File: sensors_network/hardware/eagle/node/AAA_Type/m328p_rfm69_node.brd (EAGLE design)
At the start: 50.8 x 41.9 mm, 37 parts, among them IC2 L6920, SW2 Node ID, U1 ATMEGA328P, U2 RFM69W, Y1 8MHz

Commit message: [sensors_network][AAA_Type] final pcb touches
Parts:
- moved R4 0.25 mm to (25.7, 6.60)
- moved JP2 0.25 mm to (19.1, 3.05)
- moved JP4 0.25 mm to (19.1, 6.35)
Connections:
- removed net D5_EXT: JP5.1, SJ1.1
- new net D6_EXT: JP5.2, SJ1.1
- net D5: now also JP5.1; no longer SJ1.2
- net D6: now also SJ1.2; no longer JP5.2
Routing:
- net D5: track 24.9 -> 8.42 mm, vias 2 -> 0
- net D5_EXT: track 9.61 -> 0.00 mm, vias 2 -> 0
- net GND: track 275.5 -> 267.9 mm
- net B1: track 12.2 -> 17.0 mm, vias 0 -> 2
- net D6: track 9.81 -> 6.36 mm
- net D6_EXT: track 0.00 -> 3.21 mm
- net SCK: track 29.4 -> 31.1 mm
- net BATT_LVL: track 38.2 -> 39.7 mm
- net CT_OUT: track 33.2 -> 34.1 mm
- net RESET: track 49.9 -> 50.6 mm
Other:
- board text added: "RF_LED|D6"
- board text removed: "RF_LED|D5"

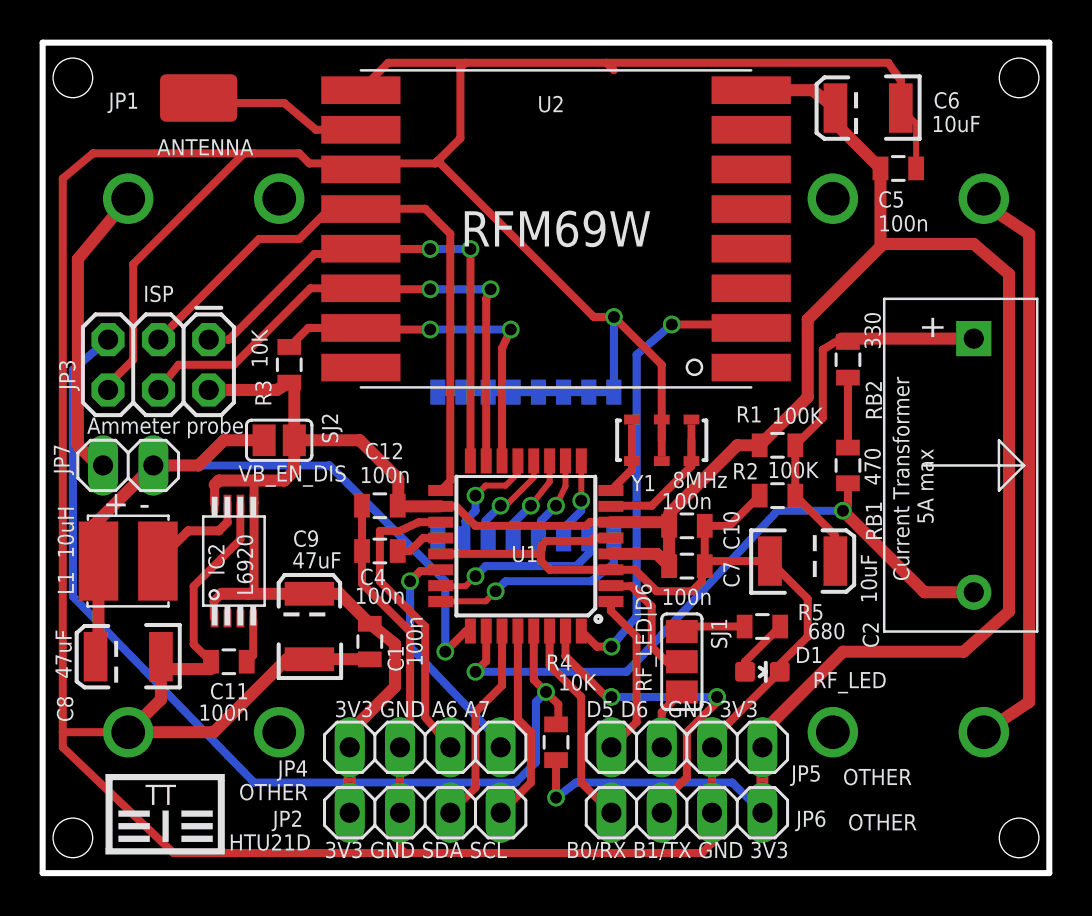
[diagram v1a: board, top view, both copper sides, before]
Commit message: [sensors_network][AAA_Type] reduced board outline dimension to fit 5x5 cm
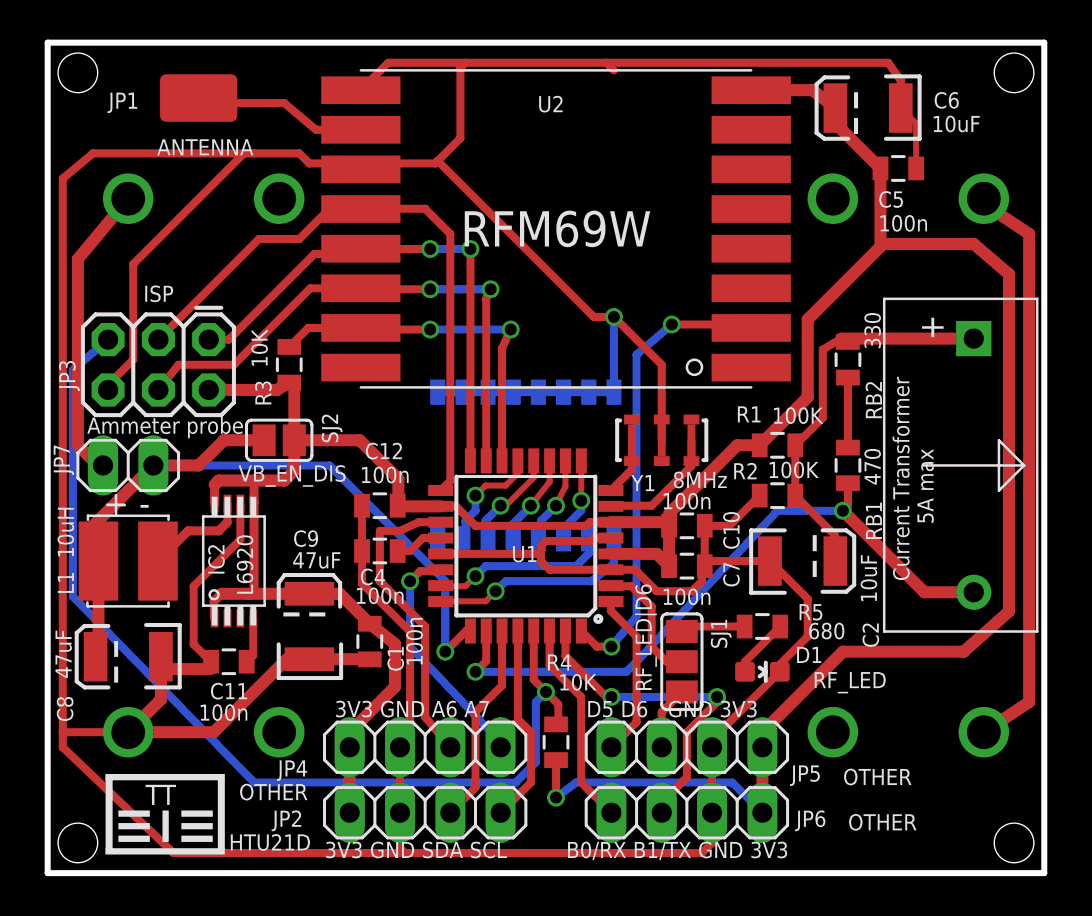
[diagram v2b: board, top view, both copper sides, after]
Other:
- board size 50.8 x 41.9 mm -> 50.3 x 41.9 mm
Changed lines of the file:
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@@
 <board>
 <plain>
-<hole x="1.27" y="40.132" drill="2"/>
-<hole x="1.27" y="1.778" drill="2"/>
-<hole x="49.022" y="1.778" drill="2"/>
-<hole x="49.022" y="40.132" drill="2"/>
-<wire x1="-0.254" y1="41.91" x2="50.546" y2="41.91" width="0.3048" layer="20"/>
-<wire x1="50.546" y1="41.91" x2="50.546" y2="0" width="0.3048" layer="20"/>
-<wire x1="50.546" y1="0" x2="-0.254" y2="0" width="0.3048" layer="20"/>
-<wire x1="-0.254" y1="0" x2="-0.254" y2="41.91" width="0.3048" layer="20"/>
+<hole x="1.524" y="40.386" drill="2"/>
+<hole x="1.524" y="1.524" drill="2"/>
+<hole x="48.768" y="1.524" drill="2"/>
+<hole x="48.768" y="40.386" drill="2"/>
+<wire x1="0" y1="41.91" x2="50.292" y2="41.91" width="0.3048" layer="20"/>
+<wire x1="50.292" y1="41.91" x2="50.292" y2="0" width="0.3048" layer="20"/>
+<wire x1="50.292" y1="0" x2="0" y2="0" width="0.3048" layer="20"/>
+<wire x1="0" y1="0" x2="0" y2="41.91" width="0.3048" layer="20"/>
 <text x="13.97" y="0.762" size="0.8128" layer="21">3V3 GND SDA SCL</text>
 <text x="14.478" y="7.874" size="0.8128" layer="21">3V3 GND A6 A7</text>
@@
 <rectangle x1="1.3716" y1="2.794" x2="4.826" y2="3.1496" layer="21" rot="R270"/>
 <text x="35.306" y="39.624" size="1.27" layer="22" rot="MR0">MySensors RFM69 Node</text>
-<text x="1.016" y="18.288" size="0.8128" layer="22" rot="MR180">Antenna Length:
+<text x="1.016" y="17.78" size="0.8128" layer="22" rot="MR180">Antenna Length:
 433 MHz -&gt; 165 mm
 868 MHz -&gt;  82 mm
@@
 </class>
 </classes>
-<designrules name="Elecrow_2-layer_PCB_eagle_rule *">
-<description language="de">&lt;b&gt;EAGLE Design Rules&lt;/b&gt;
-&lt;p&gt;
-Die Standard-Design-Rules sind so gewählt, dass sie für
-die meisten Anwendungen passen. Sollte ihre Platine
-besondere Anforderungen haben, treffen Sie die erforderlichen
-Einstellungen hier und speichern die Design Rules unter
-einem neuen Namen ab.</description>
-<description language="en">&lt;b&gt;EAGLE Design Rules&lt;/b&gt;
-&lt;p&gt;
-The default Design Rules have been set to cover
-a wide range of applications. Your particular design
-may have different requirements, so please make the
-necessary adjustments and save your customized
-design rules under a new name.</description>
-<description language="zh">&lt;b&gt;Elecrow PCB EAGLE Design Rules&lt;/b&gt;
-</description>
+<designrules name="dirt_cheap_dirty_boards.v1 *">
+<description language="en">&lt;b&gt;Dirty Cheap Dirty Board Design Rules&lt;/b&gt;
+&lt;br&gt;
+&lt;br&gt;Min width/Spacing: 5/5mil
+&lt;br&gt;Min diameter of finished hole 12mil</description>
 <param name="layerSetup" value="(1*16)"/>
-<param name="mtCopper" value="0.035mm 0.035mm 0.035mm 0.035mm 0.035mm 0.035mm 0.035mm 0.035mm 0.035mm 0.035mm 0.035mm 0.035mm 0.035mm 0.035mm 0.035mm 0.035mm"/>
-<param name="mtIsolate" value="1.6mm 1.2mm 0.2mm 0.15mm 0.2mm 0.15mm 0.2mm 0.15mm 0.2mm 0.15mm 0.2mm 0.15mm 0.2mm 0.15mm 0.2mm"/>
-<param name="mdWireWire" value="6mil"/>
-<param name="mdWirePad" value="6mil"/>
-<param name="mdWireVia" value="6mil"/>
-<param name="mdPadPad" value="6mil"/>
-<param name="mdPadVia" value="6mil"/>
-<param name="mdViaVia" value="8mil"/>
+<param name="mtCopper" value="0.035mm 0.0175mm 0.035mm 0.035mm 0.035mm 0.035mm 0.035mm 0.035mm 0.035mm 0.035mm 0.035mm 0.035mm 0.035mm 0.035mm 0.0175mm 0.035mm"/>
+<param name="mtIsolate" value="1.5mm 1.1mm 0.2mm 0.15mm 0.2mm 0.15mm 0.2mm 0.15mm 0.2mm 0.15mm 0.2mm 0.15mm 0.2mm 0.15mm 0.2mm"/>
+<param name="mdWireWire" value="5mil"/>
+<param name="mdWirePad" value="5mil"/>
+<param name="mdWireVia" value="5mil"/>
+<param name="mdPadPad" value="5mil"/>
+<param name="mdPadVia" value="5mil"/>
+<param name="mdViaVia" value="5mil"/>
 <param name="mdSmdPad" value="0mil"/>
 <param name="mdSmdVia" value="0mil"/>
@@
 <param name="mdViaViaSameLayer" value="8mil"/>
 <param name="mnLayersViaInSmd" value="2"/>
-<param name="mdCopperDimension" value="20mil"/>
+<param name="mdCopperDimension" value="10mil"/>
 <param name="mdDrill" value="10mil"/>
 <param name="mdSmdStop" value="0mil"/>
-<param name="msWidth" value="6mil"/>
+<param name="msWidth" value="5mil"/>
 <param name="msDrill" value="12mil"/>
 <param name="msMicroVia" value="12mil"/>
@@
 <param name="rvMicroViaOuter" value="0.25"/>
 <param name="rvMicroViaInner" value="0.25"/>
-<param name="rlMinPadTop" value="6mil"/>
+<param name="rlMinPadTop" value="10mil"/>
 <param name="rlMaxPadTop" value="20mil"/>
-<param name="rlMinPadInner" value="6mil"/>
+<param name="rlMinPadInner" value="10mil"/>
 <param name="rlMaxPadInner" value="20mil"/>
-<param name="rlMinPadBottom" value="6mil"/>
+<param name="rlMinPadBottom" value="10mil"/>
 <param name="rlMaxPadBottom" value="20mil"/>
 <param name="rlMinViaOuter" value="6mil"/>
@@
 <param name="mvStopFrame" value="1"/>
 <param name="mvCreamFrame" value="0"/>
-<param name="mlMinStopFrame" value="0mil"/>
-<param name="mlMaxStopFrame" value="0mil"/>
+<param name="mlMinStopFrame" value="2mil"/>
+<param name="mlMaxStopFrame" value="2mil"/>
 <param name="mlMinCreamFrame" value="0mil"/>
 <param name="mlMaxCreamFrame" value="0mil"/>
-<param name="mlViaStopLimit" value="100mil"/>
+<param name="mlViaStopLimit" value="25mil"/>
 <param name="srRoundness" value="0"/>
 <param name="srMinRoundness" value="0mil"/>
@@
 <wire x1="8.382" y1="7.112" x2="4.064" y2="7.112" width="0.6096" layer="1"/>
 <polygon width="0.4064" layer="1" isolate="0.4064" thermals="no">
-<vertex x="-0.254" y="41.91"/>
-<vertex x="50.546" y="41.91"/>
-<vertex x="50.546" y="0"/>
-<vertex x="-0.254" y="0"/>
+<vertex x="0" y="41.91"/>
+<vertex x="50.292" y="41.91"/>
+<vertex x="50.292" y="0"/>
+<vertex x="0" y="0"/>
 </polygon>
 </signal>
